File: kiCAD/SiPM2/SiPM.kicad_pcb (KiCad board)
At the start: 2 copper layers, 19.4 x 10.5 mm, 4 parts, among them J1 CON4, J2 CON4

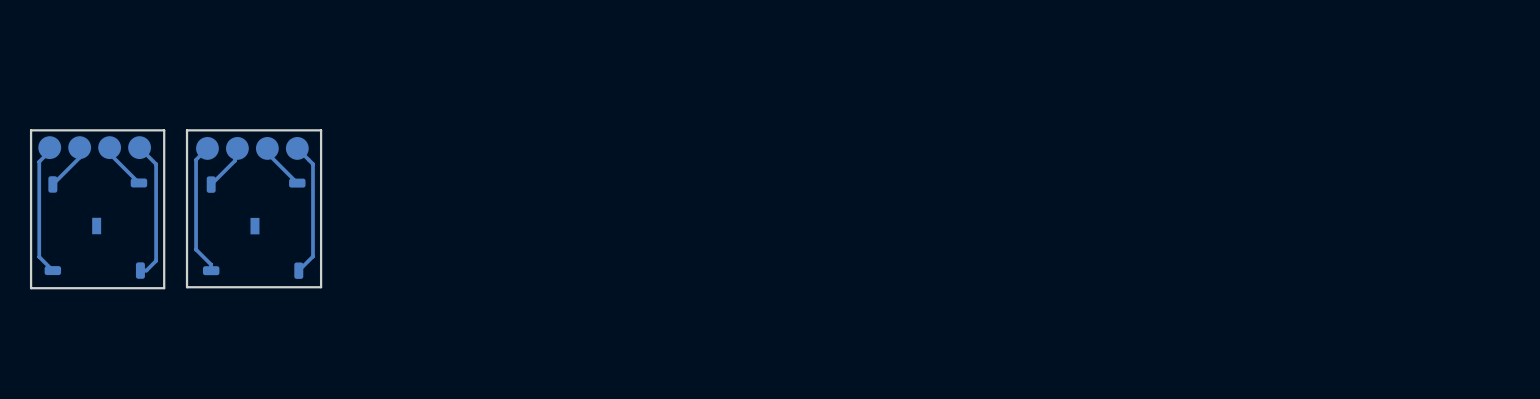
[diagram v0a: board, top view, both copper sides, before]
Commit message: удалено:       Android/AndroidDoZer/.idea/jarRepositories.xml 	изменено:      Android/AndroidDoZer/gradle/wrapper/gradle-wrapper.properties 	изменено:      kiCAD/ERQ15_11-6060-SiPM/ERQ15_11-6060-SiPM.kicad_prl 	изменено:      kiCAD/SC-STM32L412K8-light_v2/SC-STM32L412K8.kicad_prl 	изменено:      kiCAD/SiPM2/SiPM.kicad_pcb
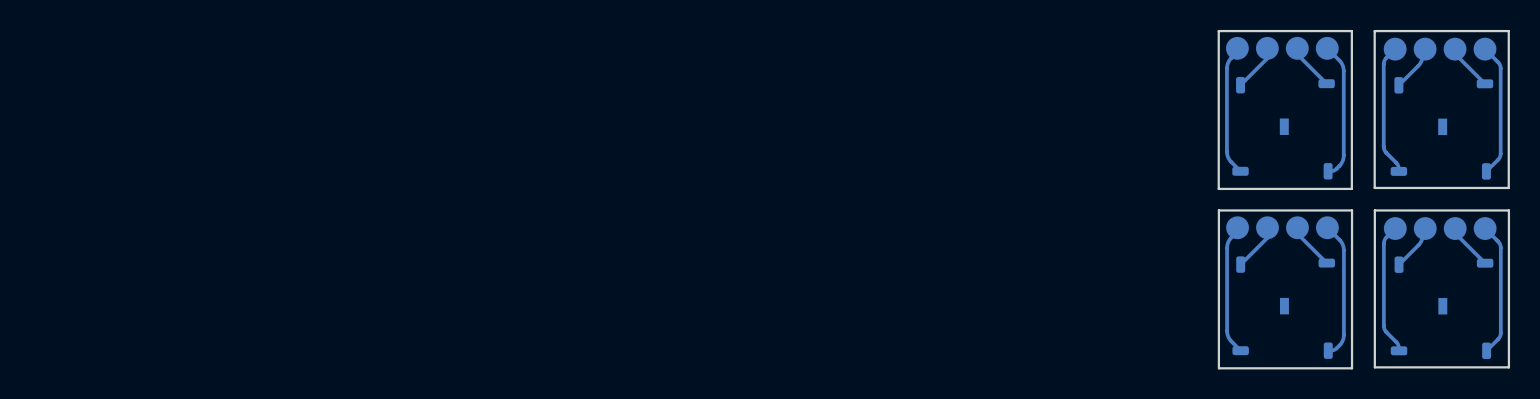
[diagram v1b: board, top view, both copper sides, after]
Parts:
- added D1: FC-60035, My-library:FC-60035, B.Cu at (103.1, 59.7)
- added D2: FC-60035, My-library:FC-60035, B.Cu at (113.6, 59.7)
- added J1: CON4, My-library:CON4, B.Cu at (102.9, 54.4)
- added J2: CON4, My-library:CON4, B.Cu at (113.5, 54.4)
- moved D1 79.6 mm to (103.1, 47.7)
- moved D2 79.6 mm to (113.6, 47.7)
- moved J1 79.6 mm to (102.9, 42.4)
- moved J2 79.6 mm to (113.5, 42.5)
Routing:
- net Net-(D1-Pad4): track 9.33 -> 18.4 mm
- net Net-(D2-Pad4): track 8.99 -> 17.9 mm
- net Net-(D2-Pad1): track 8.90 -> 17.6 mm
- net Net-(D1-Pad1): track 8.88 -> 17.6 mm
- net Net-(D1-Pad2): track 3.20 -> 6.41 mm
- net Net-(D1-Pad3): track 3.17 -> 6.34 mm
- net Net-(D2-Pad3): track 3.14 -> 6.29 mm
- net Net-(D2-Pad2): track 3.14 -> 6.19 mm
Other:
- board size 19.4 x 10.5 mm -> 19.4 x 22.5 mm
- net class Default removed
